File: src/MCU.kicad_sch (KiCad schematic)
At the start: 19 parts, among them SW201 SW_Push, SW202 SW_Push, U201 ESP32-C3-WROOM-02, U202 TLV1117LV33

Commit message: Mod: Checked a few things and added the power limitation text to the LEDs page
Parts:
- renumbered C209 to C203, C208 to C204, C203 to C205, C204 to C206, C205 to C207, C206 to C208, C207 to C209, R202 to R201, R201 to R202

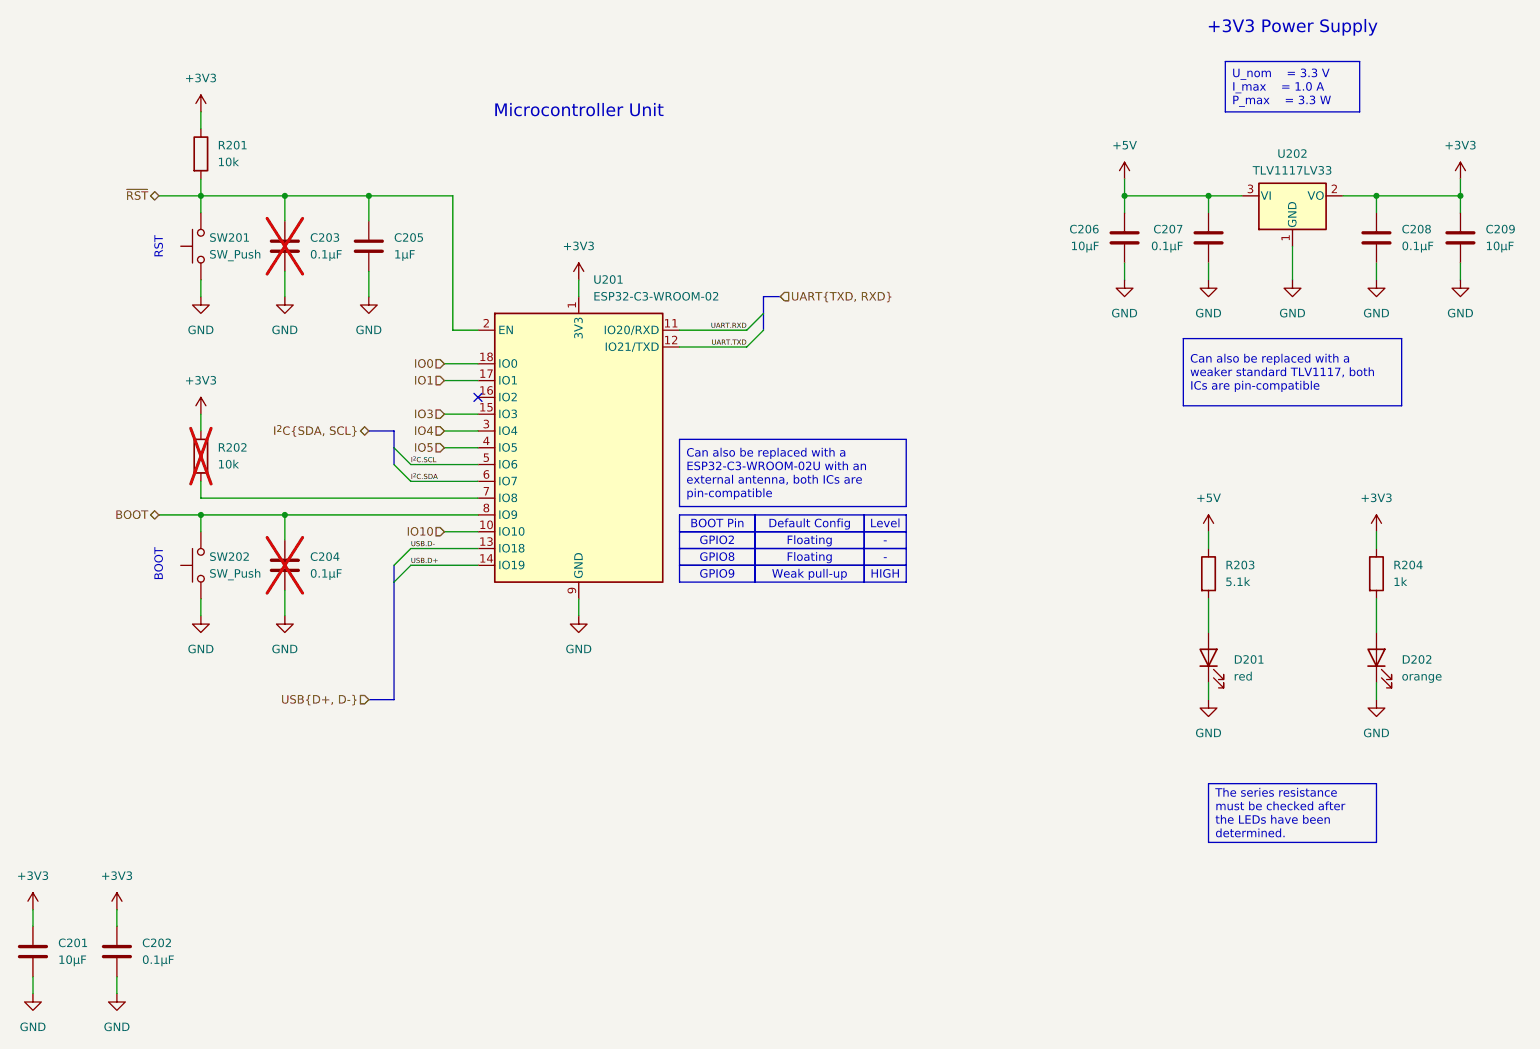
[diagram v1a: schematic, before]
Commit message: Mod: Changed the page number of the MCU and USB page
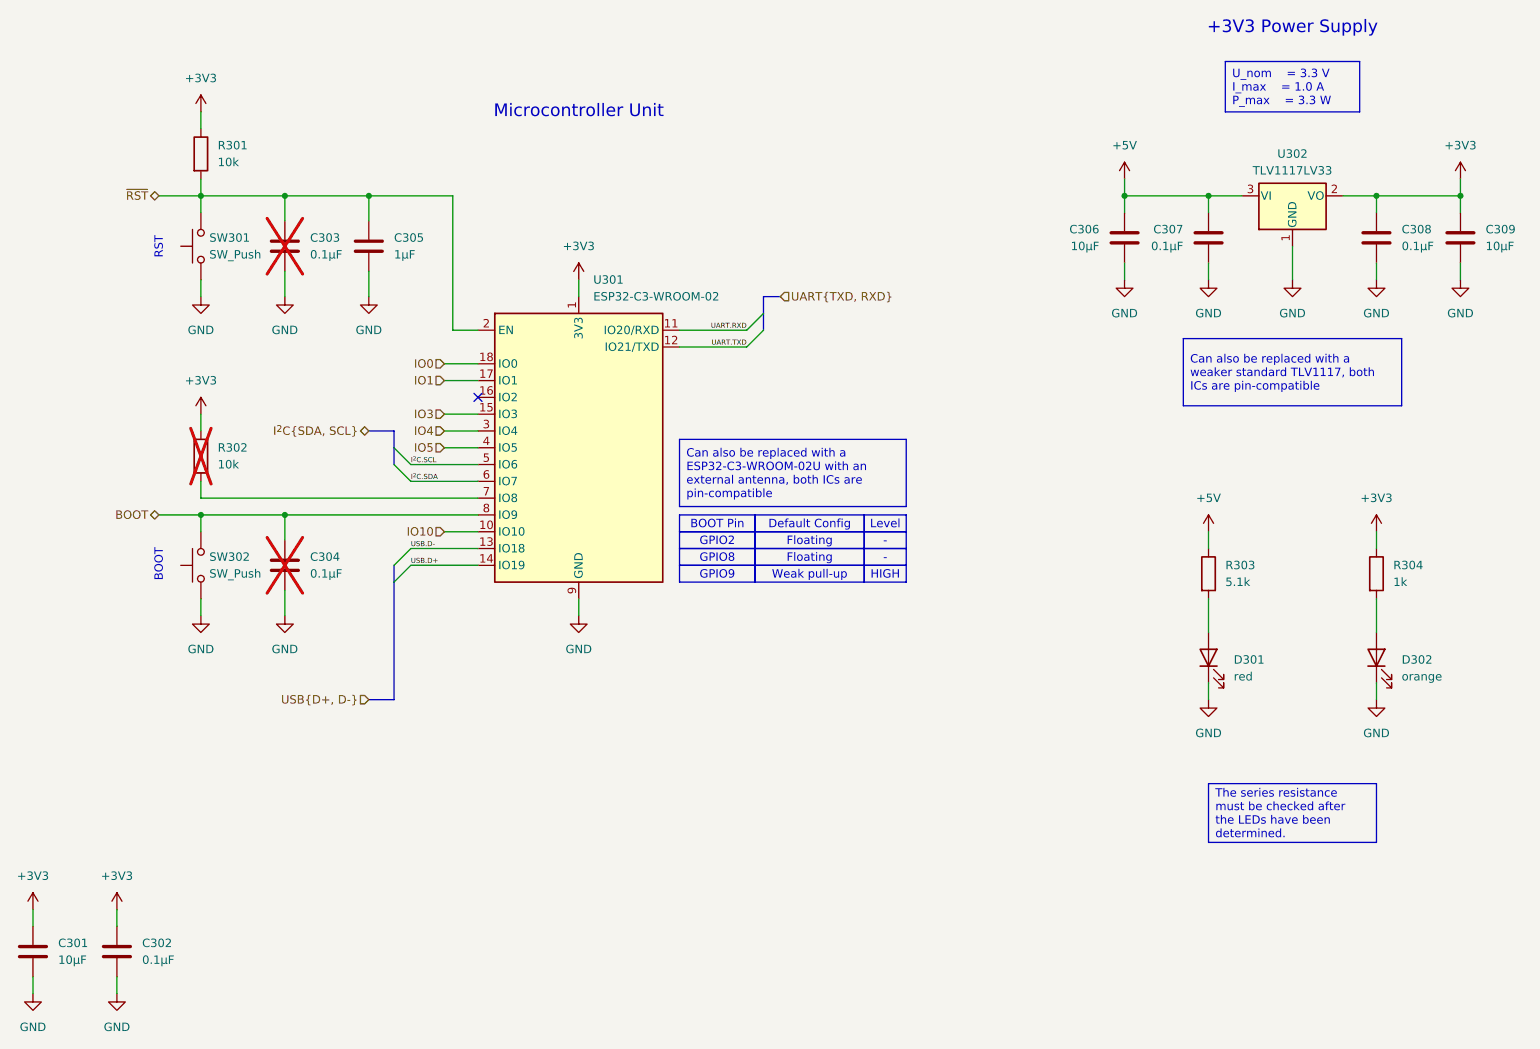
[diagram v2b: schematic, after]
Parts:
- renumbered C201 to C301, C202 to C302, C203 to C303, C204 to C304, C205 to C305, C206 to C306, C207 to C307, C208 to C308, C209 to C309, D201 to D301, D202 to D302, R201 to R301, R202 to R302, R203 to R303, R204 to R304, SW201 to SW301, SW202 to SW302, U201 to U301, U202 to U302

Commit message: Add: Vendor no. and footprints
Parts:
- C301, C306, C309: footprint (none) -> Capacitor_SMD:C_0805_2012Metric_Pad1.18x1.45mm_HandSolder; Manufacturer (none) -> -; Manufacturer Part no. (none) -> -; Vendor 1 (none) -> Digikey; Vendor 1 Part no. (none) -> 1276-1096-1-ND; Vendor 2 (none) -> LCSC
- C302, C303, C304, C307, C308: footprint (none) -> Capacitor_SMD:C_0805_2012Metric_Pad1.18x1.45mm_HandSolder; Manufacturer (none) -> -; Manufacturer Part no. (none) -> -; Vendor 1 (none) -> Digikey; Vendor 1 Part no. (none) -> 1276-2444-1-ND; Vendor 2 (none) -> LCSC
- C305: footprint (none) -> Capacitor_SMD:C_0805_2012Metric_Pad1.18x1.45mm_HandSolder; Manufacturer (none) -> -; Manufacturer Part no. (none) -> -; Vendor 1 (none) -> Digikey; Vendor 1 Part no. (none) -> 1276-1275-2-ND; Vendor 2 (none) -> LCSC
- D301: footprint (none) -> LED_SMD:LED_0805_2012Metric_Pad1.15x1.40mm_HandSolder; Manufacturer (none) -> -; Manufacturer Part no. (none) -> -; Vendor 1 (none) -> Digikey; Vendor 1 Part no. (none) -> 160-1427-1-ND; Vendor 2 (none) -> LCSC
- D302: footprint (none) -> LED_SMD:LED_0805_2012Metric_Pad1.15x1.40mm_HandSolder; Manufacturer (none) -> -; Manufacturer Part no. (none) -> -; Vendor 1 (none) -> Digikey; Vendor 1 Part no. (none) -> 160-1413-1-ND; Vendor 2 (none) -> LCSC
- R301, R302: footprint (none) -> Resistor_SMD:R_0805_2012Metric_Pad1.20x1.40mm_HandSolder; Manufacturer (none) -> -; Manufacturer Part no. (none) -> -; Vendor 1 (none) -> Digikey; Vendor 1 Part no. (none) -> 311-10.0KCRCT-ND; Vendor 2 (none) -> LCSC
- R303: footprint (none) -> Resistor_SMD:R_0805_2012Metric_Pad1.20x1.40mm_HandSolder; Manufacturer (none) -> -; Manufacturer Part no. (none) -> -; Vendor 1 (none) -> Digikey; Vendor 1 Part no. (none) -> 311-5.10KCRCT-ND; Vendor 2 (none) -> LCSC
- R304: footprint (none) -> Resistor_SMD:R_0805_2012Metric_Pad1.20x1.40mm_HandSolder; Manufacturer (none) -> -; Manufacturer Part no. (none) -> -; Vendor 1 (none) -> Digikey; Vendor 1 Part no. (none) -> 311-1.00KCRCT-ND; Vendor 2 (none) -> LCSC
- SW301, SW302: footprint (none) -> Button_Switch_SMD:SW_SPST_PTS810; Manufacturer (none) -> -; Manufacturer Part no. (none) -> -; Vendor 1 (none) -> Digikey; Vendor 1 Part no. (none) -> CKN10503CT-ND; Vendor 2 (none) -> LCSC
- U302: footprint (none) -> Package_TO_SOT_SMD:SOT-223-3_TabPin2

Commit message: Mod: Changed parts to match with both vendors
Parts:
- C301, C306, C309: Manufacturer - -> Samsung Electro-Mechanics; Manufacturer Part no. - -> CL21A106KOQNNNE; Vendor 2 Part no. (none) -> C1713
- C302, C303, C304, C307, C308: Manufacturer - -> Samsung Electro-Mechanics; Manufacturer Part no. - -> CL21B104KBCNFNC; Vendor 2 Part no. (none) -> C318718
- C305: Manufacturer - -> Samsung Electro-Mechanics; Manufacturer Part no. - -> CL21B105KPFNNNE; Vendor 2 Part no. (none) -> C107367
- D301: Manufacturer - -> Lite-On Inc.; Manufacturer Part no. - -> LTST-C171KRKT; Vendor 2 Part no. (none) -> C284871
- D302: Manufacturer - -> Lite-On Inc.; Manufacturer Part no. - -> LTST-C170KFKT; Vendor 2 Part no. (none) -> C284931
- R301, R302: Manufacturer - -> YAGEO; Manufacturer Part no. - -> RC0805FR-0710KL; Vendor 2 Part no. (none) -> C84376
- R303: Manufacturer - -> YAGEO; Manufacturer Part no. - -> RC0805FR-075K1L; Vendor 2 Part no. (none) -> C84375
- R304: Manufacturer - -> YAGEO; Manufacturer Part no. - -> RC0805FR-071KL; Vendor 2 Part no. (none) -> C95781
- SW301, SW302: Manufacturer - -> C&K; Manufacturer Part no. - -> PTS810 SJK 250 SMTR LFS; Vendor 2 Part no. (none) -> C221896
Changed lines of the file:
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@@
 	(title_block
 		(title "Wordclock - Microcontroller Unit & Power Supply")
-		(date "2024-10-27")
+		(date "2024-10-29")
 		(rev "A")
 		(company "ElektroNik Zoller")
@@
 			)
 		)
-		(property "Manufacturer" "-"
+		(property "Manufacturer" "Samsung Electro-Mechanics"
 			(at 241.3 69.85 0)
 			(effects
@@
 			)
 		)
-		(property "Manufacturer Part no." "-"
+		(property "Manufacturer Part no." "CL21A106KOQNNNE"
 			(at 241.3 69.85 0)
 			(effects
@@
 			)
 		)
+		(property "Vendor 2 Part no." "C1713"
+			(at 241.3 69.85 0)
+			(effects
+				(font
+					(size 1.27 1.27)
+				)
+				(hide yes)
+			)
+		)
 		(pin "2"
 		)
@@
 			)
 		)
-		(property "Manufacturer" "-"
+		(property "Manufacturer" "C&K"
 			(at 50.8 71.12 0)
 			(effects
@@
 			)
 		)
-		(property "Manufacturer Part no." "-"
+		(property "Manufacturer Part no." "PTS810 SJK 250 SMTR LFS"
 			(at 50.8 71.12 0)
 			(effects
@@
 			)
 		)
+		(property "Vendor 2 Part no." "C221896"
+			(at 50.8 71.12 0)
+			(effects
+				(font
+					(size 1.27 1.27)
+				)
+				(hide yes)
+			)
+		)
 		(pin "2"
 		)
@@
 			)
 		)
-		(property "Manufacturer" "-"
+		(property "Manufacturer" "Samsung Electro-Mechanics"
 			(at 203.2 69.85 0)
 			(effects
@@
 			)
 		)
-		(property "Manufacturer Part no." "-"
+		(property "Manufacturer Part no." "CL21B104KBCNFNC"
 			(at 203.2 69.85 0)
 			(effects
@@
 			)
 		)
+		(property "Vendor 2 Part no." "C318718"
+			(at 203.2 69.85 0)
+			(effects
+				(font
+					(size 1.27 1.27)
+				)
+				(hide yes)
+			)
+		)
 		(pin "2"
 		)
@@
 			)
 		)
-		(property "Manufacturer" "-"
+		(property "Manufacturer" "YAGEO"
 			(at 50.8 102.87 0)
 			(effects
@@
 			)
 		)
-		(property "Manufacturer Part no." "-"
+		(property "Manufacturer Part no." "RC0805FR-0710KL"
 			(at 50.8 102.87 0)
 			(effects
@@
 			)
 		)
+		(property "Vendor 2 Part no." "C84376"
+			(at 50.8 102.87 0)
+			(effects
+				(font
+					(size 1.27 1.27)
+				)
+				(hide yes)
+			)
+		)
 		(pin "2"
 		)
@@
 			)
 		)
-		(property "Manufacturer" "-"
+		(property "Manufacturer" "C&K"
 			(at 50.8 119.38 0)
 			(effects
@@
 			)
 		)
-		(property "Manufacturer Part no." "-"
+		(property "Manufacturer Part no." "PTS810 SJK 250 SMTR LFS"
 			(at 50.8 119.38 0)
 			(effects
@@
 			)
 		)
+		(property "Vendor 2 Part no." "C221896"
+			(at 50.8 119.38 0)
+			(effects
+				(font
+					(size 1.27 1.27)
+				)
+				(hide yes)
+			)
+		)
 		(pin "2"
 		)
@@
 			)
 		)
-		(property "Manufacturer" "-"
+		(property "Manufacturer" "Lite-On Inc."
 			(at 203.2 133.35 0)
 			(effects
@@
 			)
 		)
-		(property "Manufacturer Part no." "-"
+		(property "Manufacturer Part no." "LTST-C171KRKT"
 			(at 203.2 133.35 0)
 			(effects
@@
 			)
 		)
+		(property "Vendor 2 Part no." "C284871"
+			(at 203.2 133.35 0)
+			(effects
+				(font
+					(size 1.27 1.27)
+				)
+				(hide yes)
+			)
+		)
 		(pin "1"
 		)
@@
 			)
 		)
-		(property "Manufacturer" "-"
+		(property "Manufacturer" "Lite-On Inc."
 			(at 228.6 133.35 0)
 			(effects
@@
 			)
 		)
-		(property "Manufacturer Part no." "-"
+		(property "Manufacturer Part no." "LTST-C170KFKT"
 			(at 228.6 133.35 0)
 			(effects
@@
 			)
 		)
+		(property "Vendor 2 Part no." "C284931"
+			(at 228.6 133.35 0)
+			(effects
+				(font
+					(size 1.27 1.27)
+				)
+				(hide yes)
+			)
+		)
 		(pin "1"
 		)
@@
 			)
 		)
-		(property "Manufacturer" "-"
+		(property "Manufacturer" "Samsung Electro-Mechanics"
 			(at 63.5 71.12 0)
 			(effects
@@
 			)
 		)
-		(property "Manufacturer Part no." "-"
+		(property "Manufacturer Part no." "CL21B104KBCNFNC"
 			(at 63.5 71.12 0)
 			(effects
@@
 			)
 		)
-		(property "Vendor 2 Part no." ""
+		(property "Vendor 2 Part no." "C318718"
 			(at 63.5 71.12 0)
 			(effects
@@
 			)
 		)
-		(property "Manufacturer" "-"
+		(property "Manufacturer" "YAGEO"
 			(at 228.6 120.65 0)
 			(effects
@@
 			)
 		)
-		(property "Manufacturer Part no." "-"
+		(property "Manufacturer Part no." "RC0805FR-071KL"
 			(at 228.6 120.65 0)
 			(effects
@@
 			)
 		)
+		(property "Vendor 2 Part no." "C95781"
+			(at 228.6 120.65 0)
+			(effects
+				(font
+					(size 1.27 1.27)
+				)
+				(hide yes)
+			)
+		)
 		(pin "2"
 		)
@@
 			)
 		)
-		(property "Manufacturer" "-"
+		(property "Manufacturer" "Samsung Electro-Mechanics"
 			(at 38.1 177.8 0)
 			(effects
@@
 			)
 		)
-		(property "Manufacturer Part no." "-"
+		(property "Manufacturer Part no." "CL21B104KBCNFNC"
 			(at 38.1 177.8 0)
 			(effects
@@
 			)
 		)
+		(property "Vendor 2 Part no." "C318718"
+			(at 38.1 177.8 0)
+			(effects
+				(font
+					(size 1.27 1.27)
+				)
+				(hide yes)
+			)
+		)
 		(pin "2"
 		)
@@
 			)
 		)
-		(property "Manufacturer" "-"
+		(property "Manufacturer" "Samsung Electro-Mechanics"
 			(at 25.4 177.8 0)
 			(effects
@@
 			)
 		)
-		(property "Manufacturer Part no." "-"
+		(property "Manufacturer Part no." "CL21A106KOQNNNE"
 			(at 25.4 177.8 0)
 			(effects
@@
 			)
 		)
+		(property "Vendor 2 Part no." "C1713"
+			(at 25.4 177.8 0)
+			(effects
+				(font
+					(size 1.27 1.27)
+				)
+				(hide yes)
+			)
+		)
 		(pin "2"
 		)
@@
 			)
 		)
-		(property "Manufacturer" "-"
+		(property "Manufacturer" "YAGEO"
 			(at 50.8 57.15 0)
 			(effects
@@
 			)
 		)
-		(property "Manufacturer Part no." "-"
+		(property "Manufacturer Part no." "RC0805FR-0710KL"
 			(at 50.8 57.15 0)
 			(effects
@@
 			)
 		)
+		(property "Vendor 2 Part no." "C84376"
+			(at 50.8 57.15 0)
+			(effects
+				(font
+					(size 1.27 1.27)
+				)
+				(hide yes)
+			)
+		)
 		(pin "2"
 		)
@@
 			)
 		)
-		(property "Manufacturer" "-"
+		(property "Manufacturer" "YAGEO"
 			(at 203.2 120.65 0)
 			(effects
@@
 			)
 		)
-		(property "Manufacturer Part no." "-"
+		(property "Manufacturer Part no." "RC0805FR-075K1L"
 			(at 203.2 120.65 0)
 			(effects
@@
 			)
 		)
+		(property "Vendor 2 Part no." "C84375"
+			(at 203.2 120.65 0)
+			(effects
+				(font
+					(size 1.27 1.27)
+				)
+				(hide yes)
+			)
+		)
 		(pin "2"
 		)
@@
 			)
 		)
-		(property "Manufacturer" "-"
+		(property "Manufacturer" "Samsung Electro-Mechanics"
 			(at 190.5 69.85 0)
 			(effects
@@
 			)
 		)
-		(property "Manufacturer Part no." "-"
+		(property "Manufacturer Part no." "CL21A106KOQNNNE"
 			(at 190.5 69.85 0)
 			(effects
@@
 			)
 		)
+		(property "Vendor 2 Part no." "C1713"
+			(at 190.5 69.85 0)
+			(effects
+				(font
+					(size 1.27 1.27)
+				)
+				(hide yes)
+			)
+		)
 		(pin "2"
 		)
@@
 			)
 		)
-		(property "Manufacturer" "-"
+		(property "Manufacturer" "Samsung Electro-Mechanics"
 			(at 63.5 119.38 0)
 			(effects
@@
 			)
 		)
-		(property "Manufacturer Part no." "-"
+		(property "Manufacturer Part no." "CL21B104KBCNFNC"
 			(at 63.5 119.38 0)
 			(effects
@@
 			)
 		)
-		(property "Vendor 2 Part no." ""
+		(property "Vendor 2 Part no." "C318718"
 			(at 63.5 119.38 0)
 			(effects
@@
 			)
 		)
-		(property "Manufacturer" "-"
+		(property "Manufacturer" "Samsung Electro-Mechanics"
 			(at 228.6 69.85 0)
 			(effects
@@
 			)
 		)
-		(property "Manufacturer Part no." "-"
+		(property "Manufacturer Part no." "CL21B104KBCNFNC"
 			(at 228.6 69.85 0)
 			(effects
@@
 			)
 		)
+		(property "Vendor 2 Part no." "C318718"
+			(at 228.6 69.85 0)
+			(effects
+				(font
+					(size 1.27 1.27)
+				)
+				(hide yes)
+			)
+		)
 		(pin "2"
 		)
@@
 			)
 		)
-		(property "Manufacturer" "-"
+		(property "Manufacturer" "Samsung Electro-Mechanics"
 			(at 76.2 71.12 0)
 			(effects
@@
 			)
 		)
-		(property "Manufacturer Part no." "-"
+		(property "Manufacturer Part no." "CL21B105KPFNNNE"
 			(at 76.2 71.12 0)
 			(effects
@@
 			(at 76.2 71.12 0)
 			(effects
+				(font
+					(size 1.27 1.27)
+				)
+				(hide yes)
+			)
+		)
+		(property "Vendor 2 Part no." "C107367"
+			(at 76.2 71.12 0)
+			(effects
